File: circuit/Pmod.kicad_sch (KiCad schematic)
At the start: 2 parts, among them J11 Pmod12P_UART, J12 Pmod12P_SPI

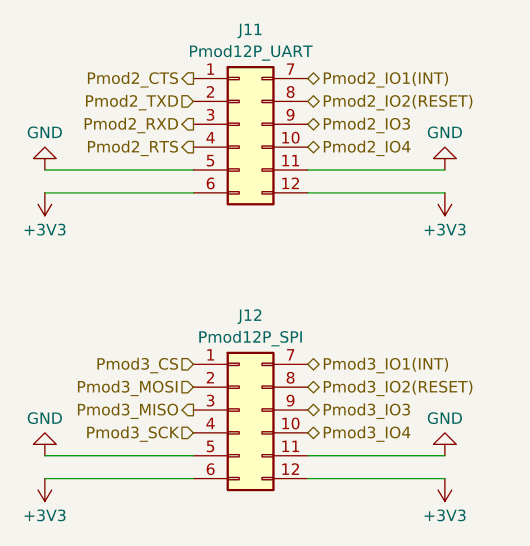
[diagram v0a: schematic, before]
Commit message: スマコンの設定変更 回路図変更
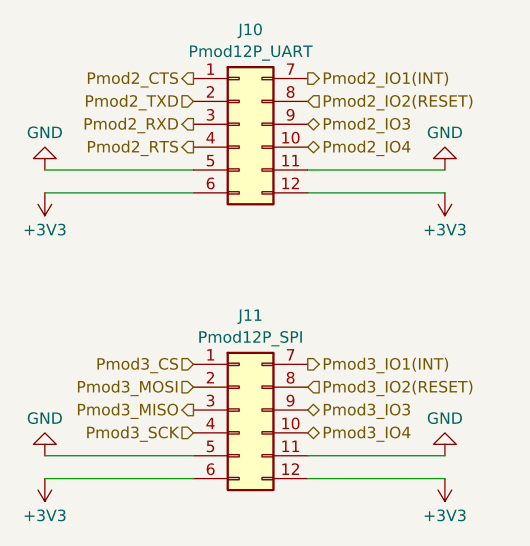
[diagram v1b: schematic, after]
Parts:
- renumbered J11 to J10, J12 to J11
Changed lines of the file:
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@@
 (kicad_sch
-	(version 20231120)
+	(version 20250114)
 	(generator "eeschema")
-	(generator_version "8.0")
+	(generator_version "9.0")
 	(paper "A4")
 	(wire
@@
 	)
 	(hierarchical_label "Pmod2_IO1(INT)"
-		(shape bidirectional)
+		(shape output)
 		(at 156.21 87.63 0)
 		(effects
@@
 	)
 	(hierarchical_label "Pmod2_IO2(RESET)"
-		(shape bidirectional)
+		(shape input)
 		(at 156.21 90.17 0)
 		(effects
@@
 	)
 	(hierarchical_label "Pmod3_IO1(INT)"
-		(shape bidirectional)
+		(shape output)
 		(at 156.21 119.38 0)
 		(effects
@@
 	)
 	(hierarchical_label "Pmod3_IO2(RESET)"
-		(shape bidirectional)
+		(shape input)
 		(at 156.21 121.92 0)
 		(effects
@@
 		(dnp no)
 		(fields_autoplaced yes)
-		(property "Reference" "#PWR088"
+		(property "Reference" "#PWR087"
 			(at 127 123.19 0)
 			(effects
@@
 			(project "mcr_MotorDriver Ver.3"
 				(path "/76b89980-2e43-4de5-94df-53966ea6619b/53053f08-0121-4498-bb15-df6666dce9cf"
-					(reference "#PWR088")
+					(reference "#PWR087")
 					(unit 1)
 				)
@@
 		(dnp no)
 		(fields_autoplaced yes)
-		(property "Reference" "#PWR091"
+		(property "Reference" "#PWR090"
 			(at 171.45 96.52 0)
 			(effects
@@
 			(project "mcr_MotorDriver Ver.3"
 				(path "/76b89980-2e43-4de5-94df-53966ea6619b/53053f08-0121-4498-bb15-df6666dce9cf"
-					(reference "#PWR091")
+					(reference "#PWR090")
 					(unit 1)
 				)
@@
 		(dnp no)
 		(fields_autoplaced yes)
-		(property "Reference" "J12"
+		(property "Reference" "J11"
 			(at 149.86 113.9655 0)
 			(effects
@@
 			(project "mcr_MotorDriver Ver.3"
 				(path "/76b89980-2e43-4de5-94df-53966ea6619b/53053f08-0121-4498-bb15-df6666dce9cf"
-					(reference "J12")
+					(reference "J11")
 					(unit 1)
 				)
@@
 		(dnp no)
 		(fields_autoplaced yes)
-		(property "Reference" "#PWR090"
+		(property "Reference" "#PWR089"
 			(at 171.45 91.44 0)
 			(effects
@@
 			(project "mcr_MotorDriver Ver.3"
 				(path "/76b89980-2e43-4de5-94df-53966ea6619b/53053f08-0121-4498-bb15-df6666dce9cf"
-					(reference "#PWR090")
+					(reference "#PWR089")
 					(unit 1)
 				)
@@
 		(dnp no)
 		(fields_autoplaced yes)
-		(property "Reference" "J11"
+		(property "Reference" "J10"
 			(at 149.86 82.2155 0)
 			(effects
@@
 			(project "mcr_MotorDriver Ver.3"
 				(path "/76b89980-2e43-4de5-94df-53966ea6619b/53053f08-0121-4498-bb15-df6666dce9cf"
-					(reference "J11")
+					(reference "J10")
 					(unit 1)
 				)
@@
 		(dnp no)
 		(fields_autoplaced yes)
-		(property "Reference" "#PWR087"
+		(property "Reference" "#PWR086"
 			(at 127 96.52 0)
 			(effects
@@
 			(project "mcr_MotorDriver Ver.3"
 				(path "/76b89980-2e43-4de5-94df-53966ea6619b/53053f08-0121-4498-bb15-df6666dce9cf"
-					(reference "#PWR087")
+					(reference "#PWR086")
 					(unit 1)
 				)
@@
 		(dnp no)
 		(fields_autoplaced yes)
-		(property "Reference" "#PWR089"
+		(property "Reference" "#PWR088"
 			(at 127 128.27 0)
 			(effects
@@
 			(project "mcr_MotorDriver Ver.3"
 				(path "/76b89980-2e43-4de5-94df-53966ea6619b/53053f08-0121-4498-bb15-df6666dce9cf"
-					(reference "#PWR089")
+					(reference "#PWR088")
 					(unit 1)
 				)
@@
 		(dnp no)
 		(fields_autoplaced yes)
-		(property "Reference" "#PWR093"
+		(property "Reference" "#PWR092"
 			(at 171.45 128.27 0)
 			(effects
@@
 			(project "mcr_MotorDriver Ver.3"
 				(path "/76b89980-2e43-4de5-94df-53966ea6619b/53053f08-0121-4498-bb15-df6666dce9cf"
-					(reference "#PWR093")
+					(reference "#PWR092")
 					(unit 1)
 				)
@@
 		(dnp no)
 		(fields_autoplaced yes)
-		(property "Reference" "#PWR092"
+		(property "Reference" "#PWR091"
 			(at 171.45 123.19 0)
 			(effects
@@
 			(project "mcr_MotorDriver Ver.3"
 				(path "/76b89980-2e43-4de5-94df-53966ea6619b/53053f08-0121-4498-bb15-df6666dce9cf"
-					(reference "#PWR092")
+					(reference "#PWR091")
 					(unit 1)
 				)
@@
 		(dnp no)
 		(fields_autoplaced yes)
-		(property "Reference" "#PWR086"
+		(property "Reference" "#PWR085"
 			(at 127 91.44 0)
 			(effects
@@
 			(project "mcr_MotorDriver Ver.3"
 				(path "/76b89980-2e43-4de5-94df-53966ea6619b/53053f08-0121-4498-bb15-df6666dce9cf"
-					(reference "#PWR086")
+					(reference "#PWR085")
 					(unit 1)
 				)
